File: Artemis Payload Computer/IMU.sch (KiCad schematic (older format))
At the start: 1 part, among them U401 FXOS8700+FXAS21002

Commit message: I think I undid this...
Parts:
- renumbered U401 to U?
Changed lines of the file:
@@
 $Descr A4 11693 8268
 encoding utf-8
-Sheet 4 5
+Sheet 4 4
 Title ""
 Date ""
@@
 $EndDescr
 $Comp
-L Artemis_Footprints:FXOS8700+FXAS21002 U401
+L Artemis_Footprints:FXOS8700+FXAS21002 U?
 U 1 1 603A9652
 P 6250 3450
-F 0 "U401" H 6275 3965 50  0000 C CNN
+F 0 "U?" H 6275 3965 50  0000 C CNN
 F 1 "FXOS8700+FXAS21002" H 6275 3874 50  0000 C CNN
 F 2 "" H 6250 3450 50  0001 C CNN

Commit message: Fuck it we're starting over. Sorry for the mess Nathan
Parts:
- gave numbers to parts that had none: 1
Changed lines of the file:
@@
 $Descr A4 11693 8268
 encoding utf-8
-Sheet 4 4
+Sheet 4 5
 Title ""
 Date ""
@@
 $EndDescr
 $Comp
-L Artemis_Footprints:FXOS8700+FXAS21002 U?
+L Artemis_Footprints:FXOS8700+FXAS21002 U401
 U 1 1 603A9652
 P 6250 3450
-F 0 "U?" H 6275 3965 50  0000 C CNN
+F 0 "U401" H 6275 3965 50  0000 C CNN
 F 1 "FXOS8700+FXAS21002" H 6275 3874 50  0000 C CNN
 F 2 "" H 6250 3450 50  0001 C CNN

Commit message: complete redo hehe
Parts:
- U?: renamed from U401; footprint (none) -> Artemis Payload Computer:IMU
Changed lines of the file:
@@
 $Descr A4 11693 8268
 encoding utf-8
-Sheet 4 5
+Sheet 4 6
 Title ""
 Date ""
@@
 $EndDescr
 $Comp
-L Artemis_Footprints:FXOS8700+FXAS21002 U401
+L Artemis_Footprints:FXOS8700+FXAS21002 U?
 U 1 1 603A9652
 P 6250 3450
-F 0 "U401" H 6275 3965 50  0000 C CNN
+F 0 "U?" H 6275 3965 50  0000 C CNN
 F 1 "FXOS8700+FXAS21002" H 6275 3874 50  0000 C CNN
-F 2 "" H 6250 3450 50  0001 C CNN
+F 2 "Artemis Payload Computer:IMU" H 6250 3450 50  0001 C CNN
 F 3 "" H 6250 3450 50  0001 C CNN
 	1    6250 3450

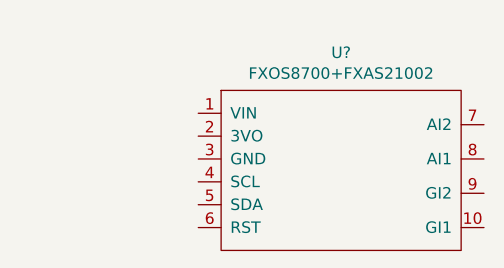
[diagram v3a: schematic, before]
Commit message: Updated Footprints
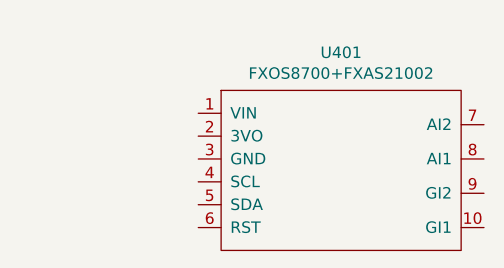
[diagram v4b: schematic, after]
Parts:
- gave numbers to parts that had none: 1
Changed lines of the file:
@@
 $EndDescr
 $Comp
-L Artemis_Footprints:FXOS8700+FXAS21002 U?
+L Artemis_Footprints:FXOS8700+FXAS21002 U401
 U 1 1 603A9652
 P 6250 3450
-F 0 "U?" H 6275 3965 50  0000 C CNN
+F 0 "U401" H 6275 3965 50  0000 C CNN
 F 1 "FXOS8700+FXAS21002" H 6275 3874 50  0000 C CNN
 F 2 "Artemis Payload Computer:IMU" H 6250 3450 50  0001 C CNN

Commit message: Shit
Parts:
- removed U401: FXOS8700+FXAS21002, Artemis Payload Computer:IMU, symbol Artemis_Footprints:FXOS8700+FXAS21002
- added U?: ICM-20948, Artemis Payload Computer:ICM-20948, symbol Artemis_Footprints:ICM-20948
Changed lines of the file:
@@
 $EndDescr
 $Comp
-L Artemis_Footprints:FXOS8700+FXAS21002 U401
-U 1 1 603A9652
-P 6250 3450
-F 0 "U401" H 6275 3965 50  0000 C CNN
-F 1 "FXOS8700+FXAS21002" H 6275 3874 50  0000 C CNN
-F 2 "Artemis Payload Computer:IMU" H 6250 3450 50  0001 C CNN
-F 3 "" H 6250 3450 50  0001 C CNN
-	1    6250 3450
+L Artemis_Footprints:ICM-20948 U?
+U 1 1 60405DA7
+P 6200 3000
+F 0 "U?" H 6225 3165 50  0000 C CNN
+F 1 "ICM-20948" H 6225 3074 50  0000 C CNN
+F 2 "Artemis Payload Computer:ICM-20948" H 6200 3000 50  0001 C CNN
+F 3 "" H 6200 3000 50  0001 C CNN
+	1    6200 3000
 	1    0    0    -1
 $EndComp

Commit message: ready for testing...
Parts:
- gave numbers to parts that had none: 1
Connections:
- net +5V: now reaches U401.1 (VIN)
- net GND: now reaches U401.3 (GND)
- net SCL0: now reaches U401.4 (SCL)
- net SDA0: now reaches U401.5 (SDA)
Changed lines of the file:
@@
 $EndDescr
 $Comp
-L Artemis_Footprints:ICM-20948 U?
+L Artemis_Footprints:ICM-20948 U401
 U 1 1 60405DA7
 P 6200 3000
-F 0 "U?" H 6225 3165 50  0000 C CNN
+F 0 "U401" H 6225 3165 50  0000 C CNN
 F 1 "ICM-20948" H 6225 3074 50  0000 C CNN
 F 2 "Artemis Payload Computer:ICM-20948" H 6200 3000 50  0001 C CNN
@@
 	1    0    0    -1
 $EndComp
+$Comp
+L power:+5V #PWR0109
+U 1 1 604076E6
+P 5600 3100
+F 0 "#PWR0109" H 5600 2950 50  0001 C CNN
+F 1 "+5V" V 5615 3228 50  0000 L CNN
+F 2 "" H 5600 3100 50  0001 C CNN
+F 3 "" H 5600 3100 50  0001 C CNN
+	1    5600 3100
+	0    -1   -1   0
+$EndComp
+$Comp
+L power:GND #PWR0110
+U 1 1 604079B0
+P 5600 3300
+F 0 "#PWR0110" H 5600 3050 50  0001 C CNN
+F 1 "GND" V 5605 3172 50  0000 R CNN
+F 2 "" H 5600 3300 50  0001 C CNN
+F 3 "" H 5600 3300 50  0001 C CNN
+	1    5600 3300
+	0    1    1    0
+$EndComp
+Wire Wire Line
+	5600 3100 5850 3100
+Wire Wire Line
+	5850 3300 5600 3300
+Text HLabel 5150 3400 0    50   Input ~ 0
+SCL0
+Text HLabel 5150 3500 0    50   Input ~ 0
+SDA0
+Wire Wire Line
+	5850 3400 5150 3400
+Wire Wire Line
+	5150 3500 5850 3500
 $EndSCHEMATC

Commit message: big commit, sorry. sd card needs finishing
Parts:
- renumbered U401 to U?
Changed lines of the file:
@@
 $Descr A4 11693 8268
 encoding utf-8
-Sheet 4 6
+Sheet 4 7
 Title ""
 Date ""
@@
 $EndDescr
 $Comp
-L Artemis_Footprints:ICM-20948 U401
+L Artemis_Footprints:ICM-20948 U?
 U 1 1 60405DA7
 P 6200 3000
-F 0 "U401" H 6225 3165 50  0000 C CNN
+F 0 "U?" H 6225 3165 50  0000 C CNN
 F 1 "ICM-20948" H 6225 3074 50  0000 C CNN
 F 2 "Artemis Payload Computer:ICM-20948" H 6200 3000 50  0001 C CNN
@@
 $EndComp
 $Comp
-L power:+5V #PWR0109
+L power:+5V #PWR?
 U 1 1 604076E6
 P 5600 3100
-F 0 "#PWR0109" H 5600 2950 50  0001 C CNN
+F 0 "#PWR?" H 5600 2950 50  0001 C CNN
 F 1 "+5V" V 5615 3228 50  0000 L CNN
 F 2 "" H 5600 3100 50  0001 C CNN
@@
 $EndComp
 $Comp
-L power:GND #PWR0110
+L power:GND #PWR?
 U 1 1 604079B0
 P 5600 3300
-F 0 "#PWR0110" H 5600 3050 50  0001 C CNN
+F 0 "#PWR?" H 5600 3050 50  0001 C CNN
 F 1 "GND" V 5605 3172 50  0000 R CNN
 F 2 "" H 5600 3300 50  0001 C CNN
